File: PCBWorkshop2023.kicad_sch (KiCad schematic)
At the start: 10 parts, among them J1 Neopixel, J2 I2C, SW1 POWER SELECT, U1 TP4056, U2 WeMos_D1_mini

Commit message: Changes with Bernd
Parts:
- added J3: Conn_01x02, Connector_PinHeader_2.54mm:PinHeader_1x02_P2.54mm_Vertical, symbol Connector_Generic:Conn_01x02
- added J4: Connections, Connector_PinHeader_2.54mm:PinHeader_1x07_P2.54mm_Vertical, symbol Connector_Generic:Conn_01x07
- J2: footprint Connector_PinHeader_2.54mm:PinHeader_1x04_P2.54mm_Vertical -> Connector_PinHeader_2.00mm:PinHeader_1x04_P2.00mm_Vertical
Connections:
- net +3V3: now also J4.2 (Pin_2)
- net +5V: now also J3.2 (Pin_2)
- net GND: now also J3.1 (Pin_1), J4.1 (Pin_1)
- net DEEPSLEEP: now reaches U2.1 (~{RST})
- net DEEPSLEEP: now also U2.3 (D0)
- net at U2.2 (A0): now also J4.7 (Pin_7)
- net at U2.4 (SCK/D5): now also J4.6 (Pin_6)
- net at U2.5 (MISO/D6): now also J4.5 (Pin_5)
- net at U2.6 (MOSI/D7): now also J4.4 (Pin_4)
- net at U2.7 (CS/D8): now also J4.3 (Pin_3)
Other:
- note removed: "TODO: - Choose a footprint for the Power Switch"
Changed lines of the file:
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@@
 (kicad_sch (version 20211123) (generator eeschema)
   (paper "A4")
-  (text "TODO:\n\n- Choose a footprint for the Power Switch" (at 58.674 70.612 0)
-    (effects (font (size 1.27 1.27)) (justify left bottom))
+  (junction (at 96.012 49.276) (diameter 0) (color 0 0 0 0)
+  )
+  (junction (at 96.012 31.496) (diameter 0) (color 0 0 0 0)
+  )
+  (wire (pts (xy 75.692 49.276) (xy 96.012 49.276))
+    (stroke (width 0) (type default) (color 0 0 0 0))
+  )
+  (wire (pts (xy 133.096 84.582) (xy 150.622 84.582))
+    (stroke (width 0) (type default) (color 0 0 0 0))
+  )
+  (wire (pts (xy 150.622 82.042) (xy 150.622 69.342))
+    (stroke (width 0) (type default) (color 0 0 0 0))
+  )
+  (wire (pts (xy 150.622 69.342) (xy 133.096 69.342))
+    (stroke (width 0) (type default) (color 0 0 0 0))
+  )
+  (wire (pts (xy 75.692 31.496) (xy 75.692 39.116))
+    (stroke (width 0) (type default) (color 0 0 0 0))
+  )
+  (wire (pts (xy 75.692 41.656) (xy 75.692 49.276))
+    (stroke (width 0) (type default) (color 0 0 0 0))
+  )
+  (wire (pts (xy 96.012 31.496) (xy 75.692 31.496))
+    (stroke (width 0) (type default) (color 0 0 0 0))
+  )
+  (wire (pts (xy 133.096 87.122) (xy 150.622 87.122))
+    (stroke (width 0) (type default) (color 0 0 0 0))
+  )
+  (wire (pts (xy 133.096 92.202) (xy 150.622 92.202))
+    (stroke (width 0) (type default) (color 0 0 0 0))
+  )
+  (wire (pts (xy 133.096 89.662) (xy 150.622 89.662))
+    (stroke (width 0) (type default) (color 0 0 0 0))
   )
   (global_label "I2C_SDA" (shape input) (at 182.372 60.198 180) (fields_autoplaced)
@@
     )
   )
+  (global_label "DEEPSLEEP" (shape input) (at 112.776 71.882 180) (fields_autoplaced)
+    (effects (font (size 1.27 1.27)) (justify right))
+    (property "Intersheet References" "${INTERSHEET_REFS}" (id 0) (at 99.7191 71.8026 0)
+      (effects (font (size 1.27 1.27)) (justify right) hide)
+    )
+  )
+  (global_label "DEEPSLEEP" (shape input) (at 133.096 71.882 0) (fields_autoplaced)
+    (effects (font (size 1.27 1.27)) (justify left))
+    (property "Intersheet References" "${INTERSHEET_REFS}" (id 0) (at 146.1529 71.9614 0)
+      (effects (font (size 1.27 1.27)) (justify left) hide)
+    )
+  )
   (global_label "I2C_CLK" (shape input) (at 182.372 57.658 180) (fields_autoplaced)
     (effects (font (size 1.27 1.27)) (justify right))
@@
     )
     (property "Datasheet" "" (id 3) (at 182.372 65.278 0)
+      (effects (font (size 1.27 1.27)) hide)
+    )
+    (pin "1")
+  )
+  (symbol (lib_id "power:GND") (at 150.622 97.282 270) (unit 1)
+    (in_bom yes) (on_board yes) (fields_autoplaced)
+    (property "Reference" "#PWR0113" (id 0) (at 144.272 97.282 0)
+      (effects (font (size 1.27 1.27)) hide)
+    )
+    (property "Value" "GND" (id 1) (at 151.384 97.2819 90)
+      (effects (font (size 1.27 1.27)) (justify left))
+    )
+    (property "Footprint" "" (id 2) (at 150.622 97.282 0)
+      (effects (font (size 1.27 1.27)) hide)
+    )
+    (property "Datasheet" "" (id 3) (at 150.622 97.282 0)
       (effects (font (size 1.27 1.27)) hide)
     )
@@
     )
   )
+  (symbol (lib_id "Connector_Generic:Conn_01x07") (at 155.702 89.662 0) (mirror x) (unit 1)
+    (in_bom yes) (on_board yes) (fields_autoplaced)
+    (property "Reference" "J4" (id 0) (at 155.702 74.93 0))
+    (property "Value" "Connections" (id 1) (at 155.702 77.47 0))
+    (property "Footprint" "Connector_PinHeader_2.54mm:PinHeader_1x07_P2.54mm_Vertical" (id 2) (at 155.702 89.662 0)
+      (effects (font (size 1.27 1.27)) hide)
+    )
+    (property "Datasheet" "~" (id 3) (at 155.702 89.662 0)
+      (effects (font (size 1.27 1.27)) hide)
+    )
+    (pin "1")
+    (pin "2")
+    (pin "3")
+    (pin "4")
+    (pin "5")
+    (pin "6")
+    (pin "7")
+  )
   (symbol (lib_id "Mechanical:MountingHole") (at 189.23 87.376 0) (unit 1)
     (in_bom yes) (on_board yes) (fields_autoplaced)
@@
       (effects (font (size 1.27 1.27)) hide)
     )
+  )
+  (symbol (lib_id "power:+3V3") (at 150.622 94.742 90) (unit 1)
+    (in_bom yes) (on_board yes)
+    (property "Reference" "#PWR0114" (id 0) (at 154.432 94.742 0)
+      (effects (font (size 1.27 1.27)) hide)
+    )
+    (property "Value" "+3V3" (id 1) (at 146.812 94.234 0))
+    (property "Footprint" "" (id 2) (at 150.622 94.742 0)
+      (effects (font (size 1.27 1.27)) hide)
+    )
+    (property "Datasheet" "" (id 3) (at 150.622 94.742 0)
+      (effects (font (size 1.27 1.27)) hide)
+    )
+    (pin "1")
   )
   (symbol (lib_id "Mechanical:MountingHole") (at 189.992 81.534 0) (unit 1)
@@
     (property "Reference" "J2" (id 0) (at 187.452 50.8 0))
     (property "Value" "I2C" (id 1) (at 187.452 53.34 0))
-    (property "Footprint" "Connector_PinHeader_2.54mm:PinHeader_1x04_P2.54mm_Vertical" (id 2) (at 187.452 62.738 0)
+    (property "Footprint" "Connector_PinHeader_2.00mm:PinHeader_1x04_P2.00mm_Vertical" (id 2) (at 187.452 62.738 0)
       (effects (font (size 1.27 1.27)) hide)
     )
@@
     (pin "1")
   )
+  (symbol (lib_id "Connector_Generic:Conn_01x02") (at 70.612 41.656 180) (unit 1)
+    (in_bom yes) (on_board yes) (fields_autoplaced)
+    (property "Reference" "J3" (id 0) (at 70.612 33.02 0))
+    (property "Value" "Conn_01x02" (id 1) (at 70.612 35.56 0))
+    (property "Footprint" "Connector_PinHeader_2.54mm:PinHeader_1x02_P2.54mm_Vertical" (id 2) (at 70.612 41.656 0)
+      (effects (font (size 1.27 1.27)) hide)
+    )
+    (property "Datasheet" "~" (id 3) (at 70.612 41.656 0)
+      (effects (font (size 1.27 1.27)) hide)
+    )
+    (pin "1")
+    (pin "2")
+  )
   (sheet_instances
     (path "/" (page "1"))
@@
       (reference "#PWR0112") (unit 1) (value "+4V") (footprint "")
     )
+    (path "/62868b2d-59ba-40f1-95d6-b00ab85d19f0"
+      (reference "#PWR0113") (unit 1) (value "GND") (footprint "")
+    )
+    (path "/933affc6-e53e-4501-ac7e-8b96cb7ccfcd"
+      (reference "#PWR0114") (unit 1) (value "+3V3") (footprint "")
+    )
     (path "/cc4858da-e012-4c55-93ac-9c3d0188091e"
       (reference "BT1") (unit 1) (value "Battery_Cell") (footprint "Connector_JST:JST_EH_S2B-EH_1x02_P2.50mm_Horizontal")
@@
     )
     (path "/a51f058c-ae9e-4d69-8e71-d5af26dc99b2"
-      (reference "J2") (unit 1) (value "I2C") (footprint "Connector_PinHeader_2.54mm:PinHeader_1x04_P2.54mm_Vertical")
+      (reference "J2") (unit 1) (value "I2C") (footprint "Connector_PinHeader_2.00mm:PinHeader_1x04_P2.00mm_Vertical")
+    )
+    (path "/f773fe60-5b71-46fc-9276-7f10955228f0"
+      (reference "J3") (unit 1) (value "Conn_01x02") (footprint "Connector_PinHeader_2.54mm:PinHeader_1x02_P2.54mm_Vertical")
+    )
+    (path "/8abf5ca8-1beb-48e3-a69f-e7076861b911"
+      (reference "J4") (unit 1) (value "Connections") (footprint "Connector_PinHeader_2.54mm:PinHeader_1x07_P2.54mm_Vertical")
     )
     (path "/c5b61907-c493-4c72-84ee-b1c385e85474"

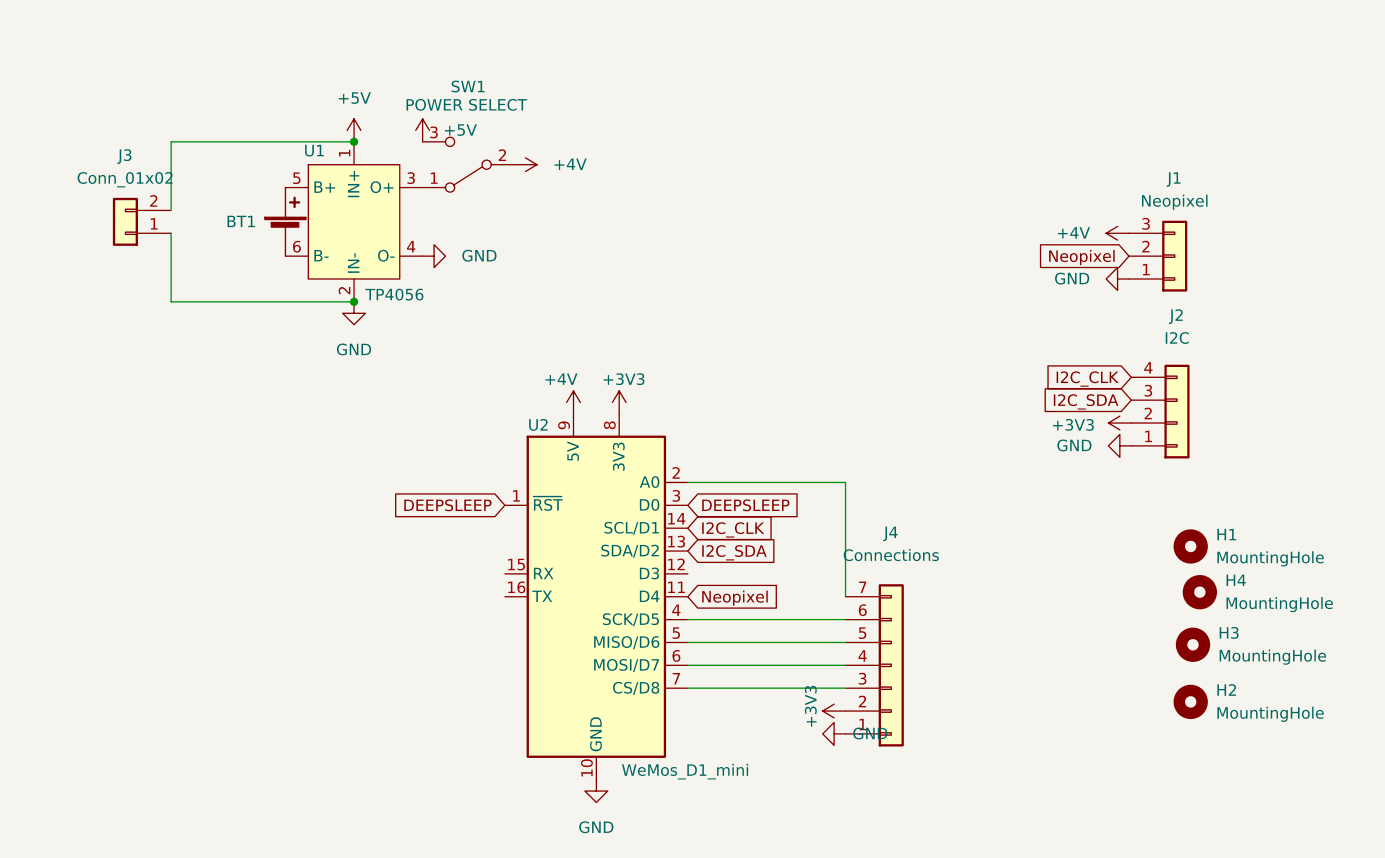
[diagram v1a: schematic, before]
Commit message: Rounded corners and switch
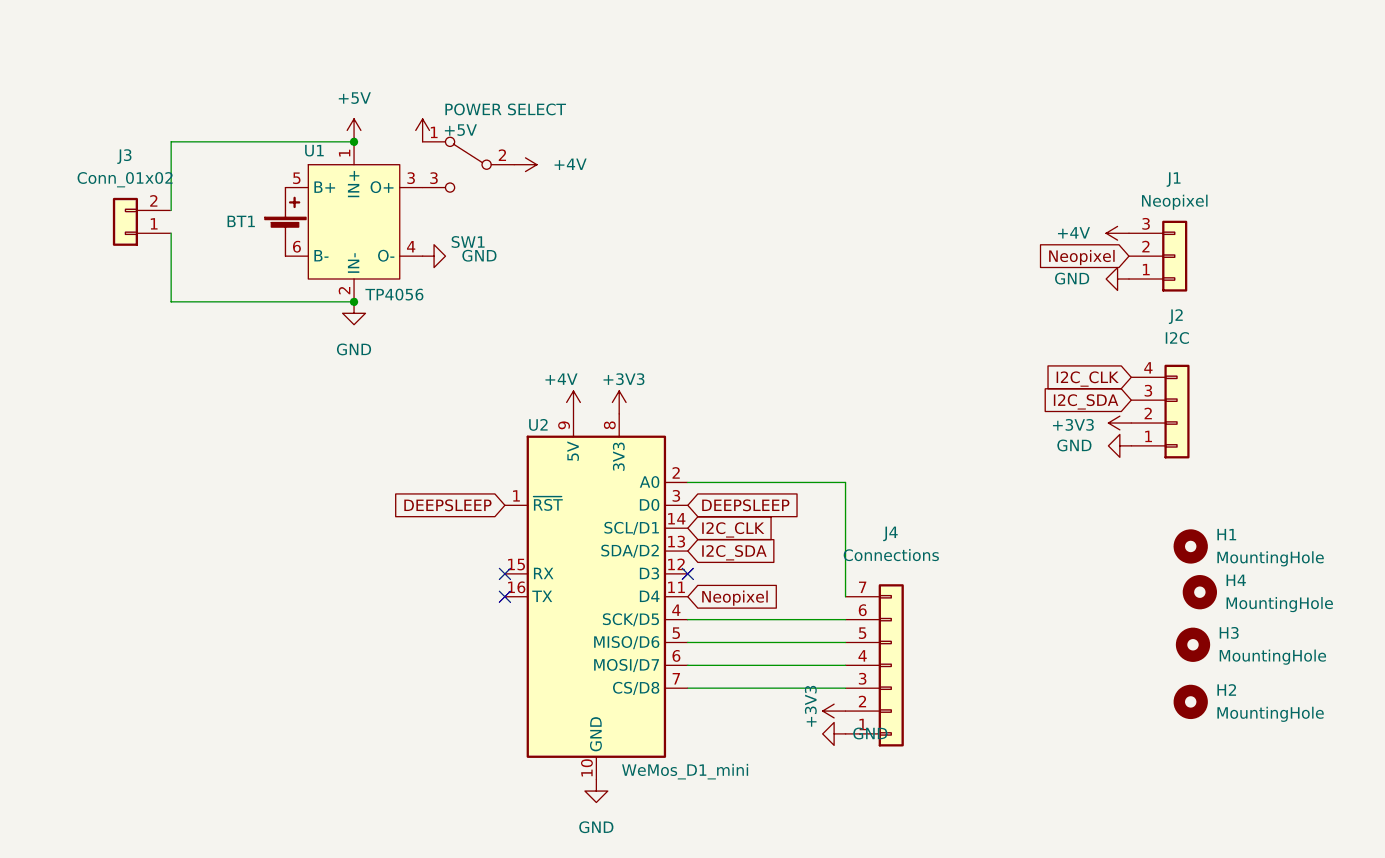
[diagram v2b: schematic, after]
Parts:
- SW1: footprint Button_Switch_THT:SW_CuK_JS202011CQN_DPDT_Straight -> Button_Switch_THT:SW_Push_1P2T_Vertical_E-Switch_800UDP8P1A1M6
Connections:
- net +5V: now also SW1.1 (A); no longer SW1.3 (C)
- net at U1.3 (O+): now also SW1.3 (C); no longer SW1.1 (A)
- no-connect marks 0 -> 3
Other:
- moved on the sheet: SW1
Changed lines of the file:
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@@
   (junction (at 96.012 31.496) (diameter 0) (color 0 0 0 0)
   )
+  (no_connect (at 133.096 79.502))
+  (no_connect (at 112.776 82.042))
+  (no_connect (at 112.776 79.502))
   (wire (pts (xy 75.692 49.276) (xy 96.012 49.276))
     (stroke (width 0) (type default) (color 0 0 0 0))
@@
     (pin "1")
   )
-  (symbol (lib_id "Switch:SW_SPDT") (at 108.712 34.036 180) (unit 1)
-    (in_bom yes) (on_board yes)
-    (property "Reference" "SW1" (id 0) (at 108.712 25.4 0))
-    (property "Value" "POWER SELECT" (id 1) (at 108.458 27.432 0))
-    (property "Footprint" "Button_Switch_THT:SW_CuK_JS202011CQN_DPDT_Straight" (id 2) (at 108.712 34.036 0)
+  (symbol (lib_id "Switch:SW_SPDT") (at 108.712 34.036 0) (mirror y) (unit 1)
+    (in_bom yes) (on_board yes)
+    (property "Reference" "SW1" (id 0) (at 108.712 42.672 0))
+    (property "Value" "POWER SELECT" (id 1) (at 112.776 27.94 0))
+    (property "Footprint" "Button_Switch_THT:SW_Push_1P2T_Vertical_E-Switch_800UDP8P1A1M6" (id 2) (at 108.712 34.036 0)
       (effects (font (size 1.27 1.27)) hide)
     )
@@
     )
     (path "/c5b61907-c493-4c72-84ee-b1c385e85474"
-      (reference "SW1") (unit 1) (value "POWER SELECT") (footprint "Button_Switch_THT:SW_CuK_JS202011CQN_DPDT_Straight")
+      (reference "SW1") (unit 1) (value "POWER SELECT") (footprint "Button_Switch_THT:SW_Push_1P2T_Vertical_E-Switch_800UDP8P1A1M6")
     )
     (path "/3f8d9778-18b4-4fc1-97b0-91bee033684b"

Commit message: Prepare for milling
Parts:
- added D1: 1N4001, Diode_THT:D_A-405_P7.62mm_Horizontal, symbol Diode:1N4001
- SW1: value POWER SELECT -> POWER; symbol Switch:SW_SPDT -> Switch:SW_SPST
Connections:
- net +4V: now also U1.3 (O+); no longer J1.3 (Pin_3), U2.9 (5V)
- net +5V: now also J1.3 (Pin_3), U2.9 (5V), D1.2 (A); no longer J3.2 (Pin_2), U1.1 (IN+)
- new net: D1.1 (K), J3.2 (Pin_2), U1.1 (IN+)
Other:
- note added: "This diode is required since when USB is connected the 5V rail of the ESP is a power output, but when running from the battery the 5V power rail is a power input"

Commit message: Improvements
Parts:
- added C1: C_Polarized, Capacitor_THT:C_Radial_D6.3mm_H11.0mm_P2.50mm, symbol Device:C_Polarized
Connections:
- net +5V: now also C1.1
- net GND: now also C1.2
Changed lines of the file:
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@@
+    (pin "1")
+  )
+  (symbol (lib_id "power:GND") (at 88.392 82.296 0) (unit 1)
+    (in_bom yes) (on_board yes) (fields_autoplaced)
+    (property "Reference" "#PWR0115" (id 0) (at 88.392 88.646 0)
+      (effects (font (size 1.27 1.27)) hide)
+    )
+    (property "Value" "GND" (id 1) (at 88.392 87.63 0))
+    (property "Footprint" "" (id 2) (at 88.392 82.296 0)
+      (effects (font (size 1.27 1.27)) hide)
+    )
+    (property "Datasheet" "" (id 3) (at 88.392 82.296 0)
+      (effects (font (size 1.27 1.27)) hide)
+    )
     (pin "1")
   )
@@
     (pin "3")
   )
+  (symbol (lib_id "power:+5V") (at 88.392 74.676 0) (unit 1)
+    (in_bom yes) (on_board yes) (fields_autoplaced)
+    (property "Reference" "#PWR0116" (id 0) (at 88.392 78.486 0)
+      (effects (font (size 1.27 1.27)) hide)
+    )
+    (property "Value" "+5V" (id 1) (at 88.392 69.85 0))
+    (property "Footprint" "" (id 2) (at 88.392 74.676 0)
+      (effects (font (size 1.27 1.27)) hide)
+    )
+    (property "Datasheet" "" (id 3) (at 88.392 74.676 0)
+      (effects (font (size 1.27 1.27)) hide)
+    )
+    (pin "1")
+  )
   (symbol (lib_id "Mechanical:MountingHole") (at 188.976 76.454 0) (unit 1)
     (in_bom yes) (on_board yes) (fields_autoplaced)
@@
     (pin "2")
   )
+  (symbol (lib_id "Device:C_Polarized") (at 88.392 78.486 0) (unit 1)
+    (in_bom yes) (on_board yes) (fields_autoplaced)
+    (property "Reference" "C1" (id 0) (at 91.44 76.3269 0)
+      (effects (font (size 1.27 1.27)) (justify left))
+    )
+    (property "Value" "C_Polarized" (id 1) (at 91.44 78.8669 0)
+      (effects (font (size 1.27 1.27)) (justify left))
+    )
+    (property "Footprint" "Capacitor_THT:C_Radial_D6.3mm_H11.0mm_P2.50mm" (id 2) (at 89.3572 82.296 0)
+      (effects (font (size 1.27 1.27)) hide)
+    )
+    (property "Datasheet" "~" (id 3) (at 88.392 78.486 0)
+      (effects (font (size 1.27 1.27)) hide)
+    )
+    (pin "1")
+    (pin "2")
+  )
   (symbol (lib_id "Device:Battery_Cell") (at 88.392 41.656 0) (unit 1)
     (in_bom yes) (on_board yes)
@@
       (reference "#PWR0114") (unit 1) (value "+3V3") (footprint "")
     )
+    (path "/279296c9-dcb4-47a5-aeec-2b087e4079bd"
+      (reference "#PWR0115") (unit 1) (value "GND") (footprint "")
+    )
+    (path "/86f0145d-843c-4344-af81-cda57453882a"
+      (reference "#PWR0116") (unit 1) (value "+5V") (footprint "")
+    )
     (path "/cc4858da-e012-4c55-93ac-9c3d0188091e"
       (reference "BT1") (unit 1) (value "Battery_Cell") (footprint "Connector_JST:JST_EH_S2B-EH_1x02_P2.50mm_Horizontal")
     )
+    (path "/c6d7917c-8840-4d2b-8483-8919f324c7e4"
+      (reference "C1") (unit 1) (value "C_Polarized") (footprint "Capacitor_THT:C_Radial_D6.3mm_H11.0mm_P2.50mm")
+    )
     (path "/8df8b067-25b8-4596-b5d1-ec8605e51747"
